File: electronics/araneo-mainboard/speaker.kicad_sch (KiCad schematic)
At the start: 2 parts, among them U1 PAM8403D, U2 MCP6002-xMC

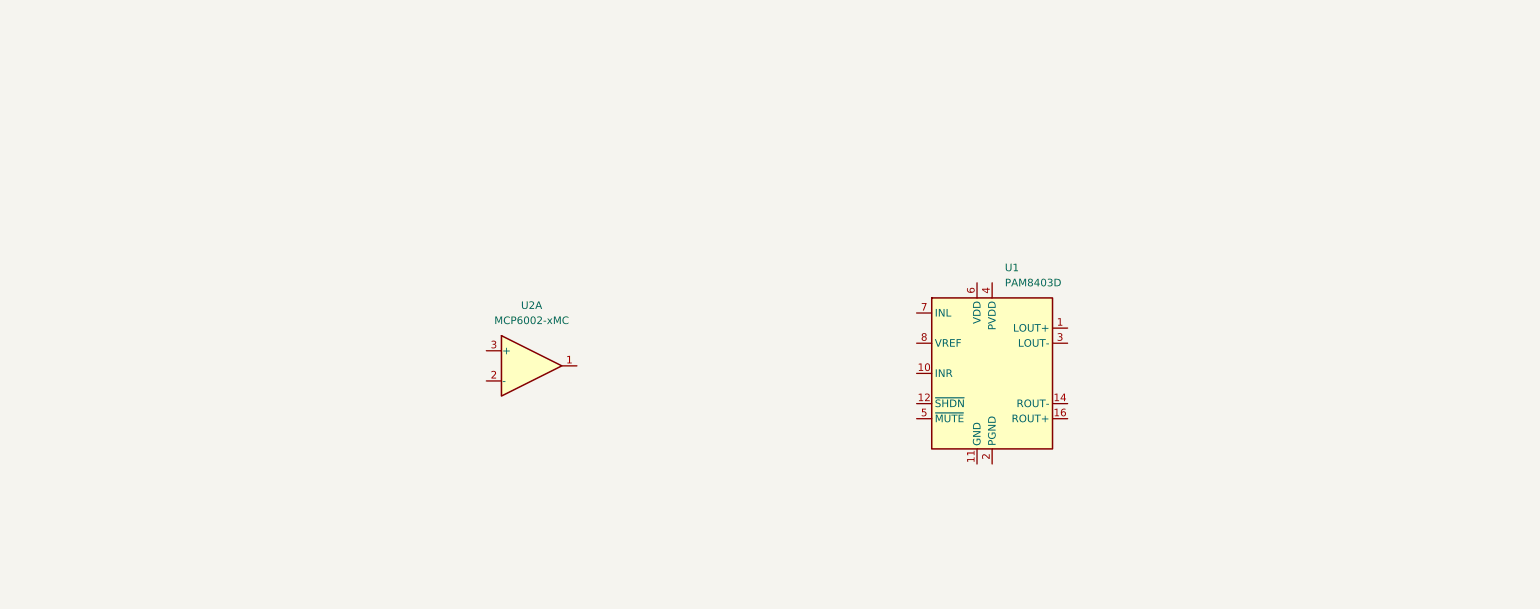
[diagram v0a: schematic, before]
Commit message: add components schematics
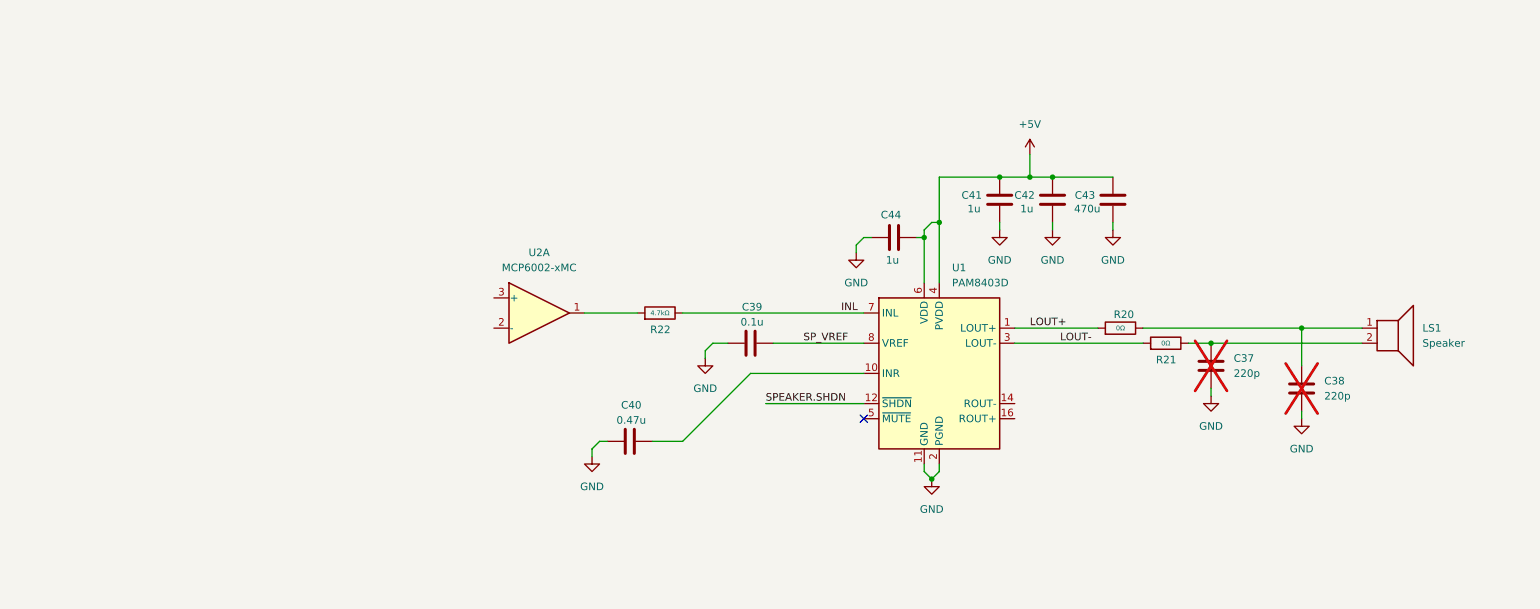
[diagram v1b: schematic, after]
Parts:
- added C37, C38: 220p, symbol Device:C
- added C39: 0.1u, symbol Device:C
- added C40: 0.47u, symbol Device:C
- added C41, C42, C44: 1u, symbol Device:C
- added C43: 470u, symbol Device:C
- added LS1: Speaker, symbol Device:Speaker
- added R20, R21: 0Ω, PCM_JLCPCB:R_0402, symbol PCM_JLCPCB-Resistors:0402,1.2kΩ
- added R22: 4.7kΩ, PCM_JLCPCB:R_0402, symbol PCM_JLCPCB-Resistors:0402,1.2kΩ
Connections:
- net LOUT+: now reaches U1.1 (LOUT+)
- net LOUT+: now also R20.1
- net at U1.10 (INR): now also C40.2
- net GND: now reaches U1.11 (GND)
- net GND: now also U1.15 (PGND), U1.2 (PGND), C37.2, C38.2, C39.1, C40.1, C41.1, C42.1, C43.1, C44.2
- net SPEAKER.SHDN: now reaches U1.12 (~{SHDN})
- net +5V: now reaches U1.13 (PVDD), U1.4 (PVDD)
- net +5V: now also U1.6 (VDD), C41.2, C42.2, C43.2, C44.1
- net LOUT-: now reaches U1.3 (LOUT-)
- net LOUT-: now also R21.1
- net INL: now reaches U1.7 (INL)
- net INL: now also R22.2
- net SP_VREF: now reaches U1.8 (VREF)
- net SP_VREF: now also C39.2
- net at U2.1: now also R22.1
- new net: C38.1, LS1.1, R20.2
- new net: C37.1, LS1.2, R21.2
- no-connect marks 0 -> 1
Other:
- moved on the sheet: U1, U2A

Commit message: add speaker schematic
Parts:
- added C45: 0.47u, symbol Device:C
- added C46: 2n, symbol Device:C
- added C47, C48, C49: 0.1u, symbol Device:C
- added R23, R24: 20kΩ, PCM_JLCPCB:R_0402, symbol PCM_JLCPCB-Resistors:0402,1.2kΩ
- added R25, R26: 10kΩ, PCM_JLCPCB:R_0402, symbol PCM_JLCPCB-Resistors:0402,1.2kΩ
- added unit 2 of U2
- added unit 3 of U2
- R22: value 4.7kΩ -> 20kΩ
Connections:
- net GND: now also C47.1, C48.1, C49.1, R26.1, U2.4 (V-), U2.9 (V-); no longer C40.1
- net SP_VREF: now also C40.1
- net at U2.1: now also C45.1, C46.2, R24.2; no longer R22.1
- net at U2.2 (-): now also C46.1, R23.2, R24.1
- net VREF_BUF: now reaches U2.3 (+)
- net VREF_BUF: now also C48.2, U2.6 (-), U2.7
- new net: C45.2, R22.1
- new net +1.65V: C47.2, R25.1, R26.2, U2.5 (+)
- new net +3.3V: C49.2, R25.2, U2.8 (V+)
- new net SPEAKER.SIGNAL: R23.1
- no-connect marks 1 -> 3
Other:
- note added: "A = R24/R23 = 1"
- note added: "Cf = 1/(2pifcRf) = 1/(2*3.14*4000*20000) = 2nF"
- moved on the sheet: C40, R22, U2A

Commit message: electronics: assign footprints
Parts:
- C37, C38, C46: footprint (none) -> PCM_JLCPCB:C_0603
- C39, C40, C41, C42, C44, C45, C47, C48, C49: footprint (none) -> PCM_JLCPCB:C_0402
- LS1: footprint (none) -> PCM_SparkFun-Connector:ScrewTerminal_1x02_P3.5mm_Blue
- R20, R21, R22, R23: footprint PCM_JLCPCB:R_0402 -> PCM_JLCPCB:R_0603
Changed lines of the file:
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@@
 			)
 		)
-		(property "Footprint" ""
+		(property "Footprint" "PCM_JLCPCB:C_0402"
 			(at 184.4548 52.07 0)
 			(hide yes)
@@
 			)
 		)
-		(property "Footprint" ""
+		(property "Footprint" "PCM_JLCPCB:C_0603"
 			(at 228.2952 91.44 0)
 			(hide yes)
@@
 			)
 		)
-		(property "Footprint" "PCM_JLCPCB:R_0402"
+		(property "Footprint" "PCM_JLCPCB:R_0603"
 			(at 60.96 74.168 90)
 			(hide yes)
@@
 			)
 		)
-		(property "Footprint" ""
+		(property "Footprint" "PCM_JLCPCB:C_0402"
 			(at 138.43 79.0448 0)
 			(hide yes)
@@
 			)
 		)
-		(property "Footprint" ""
+		(property "Footprint" "PCM_JLCPCB:C_0603"
 			(at 213.0552 87.63 0)
 			(hide yes)
@@
 			)
 		)
-		(property "Footprint" ""
+		(property "Footprint" "PCM_JLCPCB:C_0402"
 			(at 119.38 73.9648 0)
 			(hide yes)
@@
 			)
 		)
-		(property "Footprint" "PCM_JLCPCB:R_0402"
+		(property "Footprint" "PCM_JLCPCB:R_0603"
 			(at 204.47 81.788 90)
 			(hide yes)
@@
 			)
 		)
-		(property "Footprint" ""
+		(property "Footprint" "PCM_JLCPCB:C_0402"
 			(at 123.19 95.5548 0)
 			(hide yes)
@@
 			)
 		)
-		(property "Footprint" "PCM_JLCPCB:R_0402"
+		(property "Footprint" "PCM_JLCPCB:R_0603"
 			(at 196.85 79.248 90)
 			(hide yes)
@@
 			)
 		)
-		(property "Footprint" ""
+		(property "Footprint" "PCM_SparkFun-Connector:ScrewTerminal_1x02_P3.5mm_Blue"
 			(at 242.57 82.55 0)
 			(hide yes)
@@
 			)
 		)
-		(property "Footprint" ""
+		(property "Footprint" "PCM_JLCPCB:C_0402"
 			(at 78.74 115.2652 0)
 			(hide yes)
@@
 			)
 		)
-		(property "Footprint" "PCM_JLCPCB:R_0402"
+		(property "Footprint" "PCM_JLCPCB:R_0603"
 			(at 125.73 76.708 90)
 			(hide yes)
@@
 			)
 		)
-		(property "Footprint" ""
+		(property "Footprint" "PCM_JLCPCB:C_0402"
 			(at 175.5648 52.07 0)
 			(hide yes)
@@
 			)
 		)
-		(property "Footprint" ""
+		(property "Footprint" "PCM_JLCPCB:C_0402"
 			(at 29.5148 87.63 0)
 			(hide yes)
@@
 			)
 		)
-		(property "Footprint" ""
+		(property "Footprint" "PCM_JLCPCB:C_0603"
 			(at 81.28 59.9948 0)
 			(hide yes)
@@
 			)
 		)
-		(property "Footprint" ""
+		(property "Footprint" "PCM_JLCPCB:C_0402"
 			(at 65.0748 77.47 0)
 			(hide yes)
@@
 			)
 		)
-		(property "Footprint" ""
+		(property "Footprint" "PCM_JLCPCB:C_0402"
 			(at 154.94 63.1952 0)
 			(hide yes)

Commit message: add first layout
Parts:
- added R27: 0Ω, PCM_JLCPCB:R_0603, symbol PCM_JLCPCB-Resistors:0402,1.2kΩ
- C43: footprint (none) -> Capacitor_THT:CP_Radial_D10.0mm_P5.00mm
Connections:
- net +5V: now also R27.2; no longer C44.1, U1.6 (VDD)
- net LOUT+R: now reaches C38.1, LS1.1, R20.2
- net INL_R: now reaches C46.1, R23.2, R24.1, U2.2 (-)
- net LOUT-R: now reaches C37.1, LS1.2, R21.2
- net INL_I: now reaches C45.1, C46.2, R24.2, U2.1
- net INL_F: now reaches C45.2, R22.1
- net INR: now reaches C40.2, U1.10 (INR)
- new net VDD: C44.1, R27.1, U1.6 (VDD)
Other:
- moved on the sheet: LS1

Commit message: electronics: update bom
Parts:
- C43, LS1: now left out of the parts list
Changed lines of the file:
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@@
 		(body_style 1)
 		(exclude_from_sim no)
-		(in_bom yes)
+		(in_bom no)
 		(on_board yes)
 		(in_pos_files yes)
@@
 		(body_style 1)
 		(exclude_from_sim no)
-		(in_bom yes)
+		(in_bom no)
 		(on_board yes)
 		(in_pos_files yes)

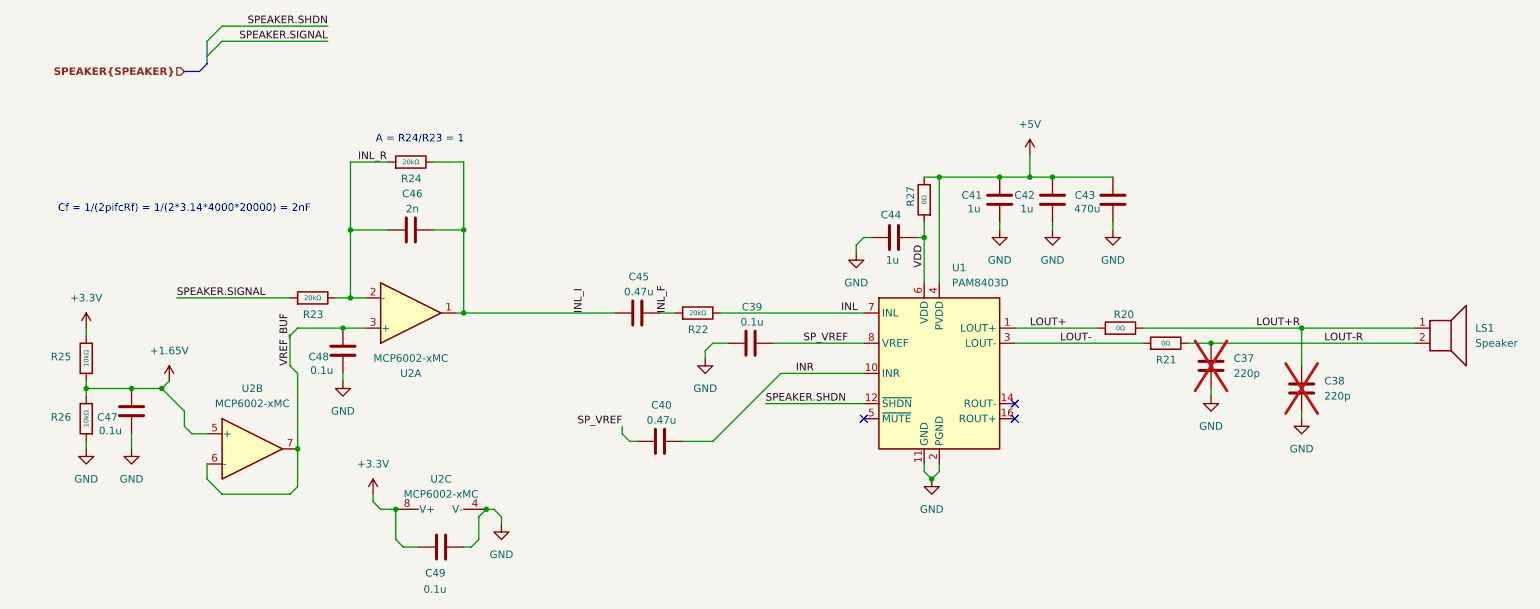
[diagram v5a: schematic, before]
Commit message: improve schematic and layout, add LCSC parts
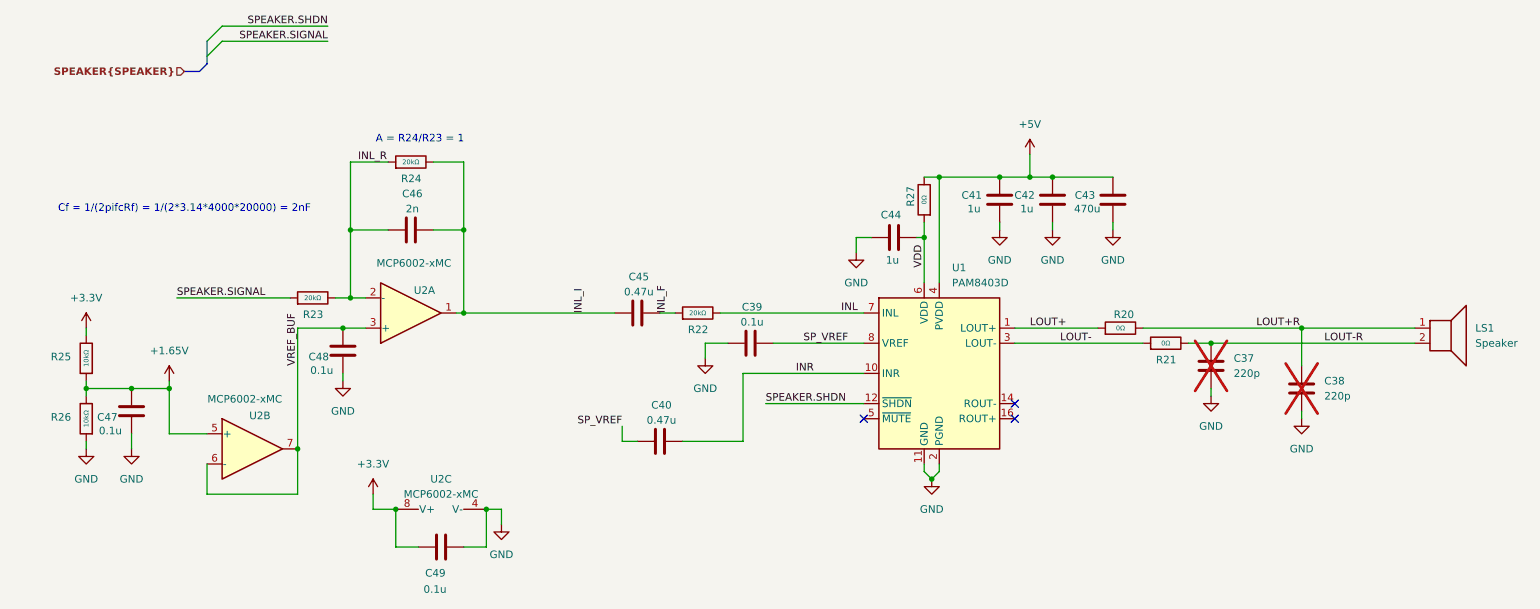
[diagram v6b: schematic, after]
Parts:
- R24: footprint PCM_JLCPCB:R_0402 -> PCM_JLCPCB:R_0603
- U2: footprint Package_DFN_QFN:DFN-8-1EP_3x2mm_P0.5mm_EP1.75x1.45mm -> PCM_JLCPCB:SOIC-8_L4.9-W3.9-P1.27-LS6.0-BL
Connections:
- net GND: no longer U2.9 (V-)
